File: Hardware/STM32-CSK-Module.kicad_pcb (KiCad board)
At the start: 2 copper layers, 32 parts, among them J1 Conn_Cortex-JTAG-10, U1 STM32F417VGT, X1 8MHz, X2 32.768kHz

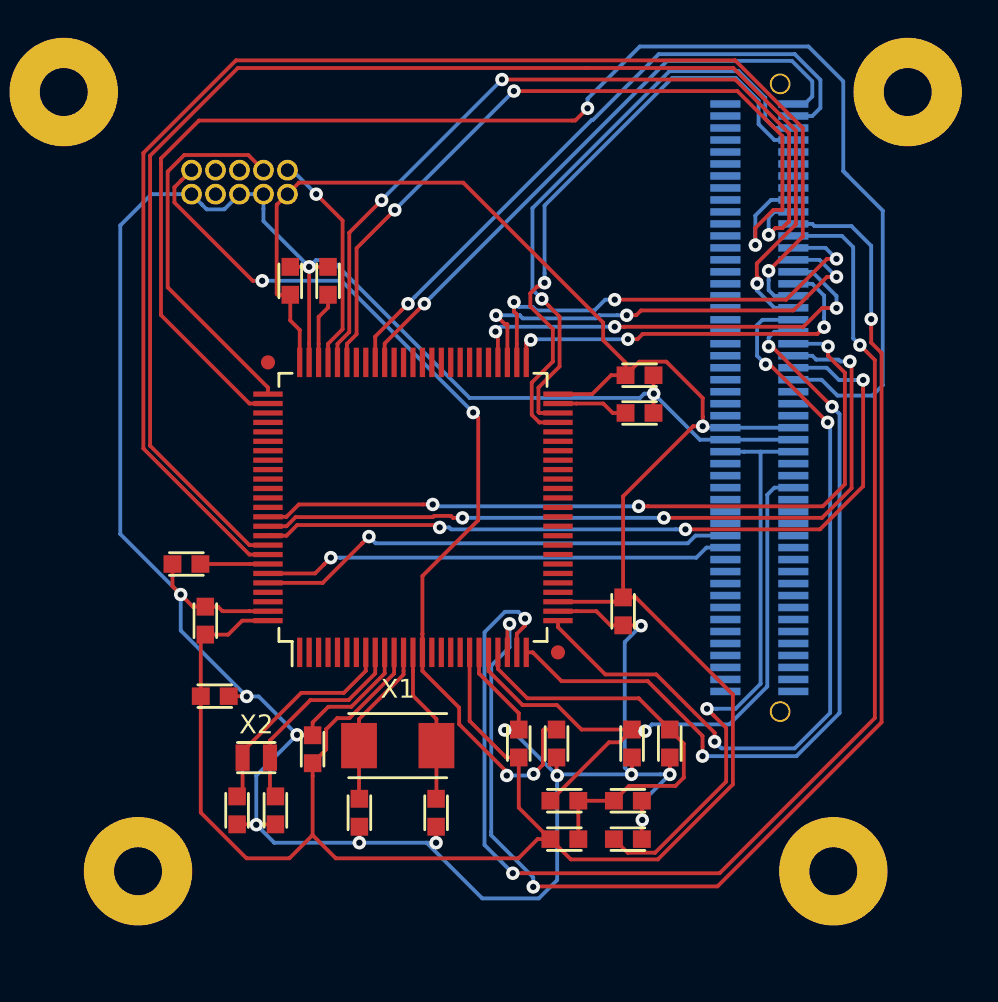
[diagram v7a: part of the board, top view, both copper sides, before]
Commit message: Progress on routing flexible GPIOs
About 50%
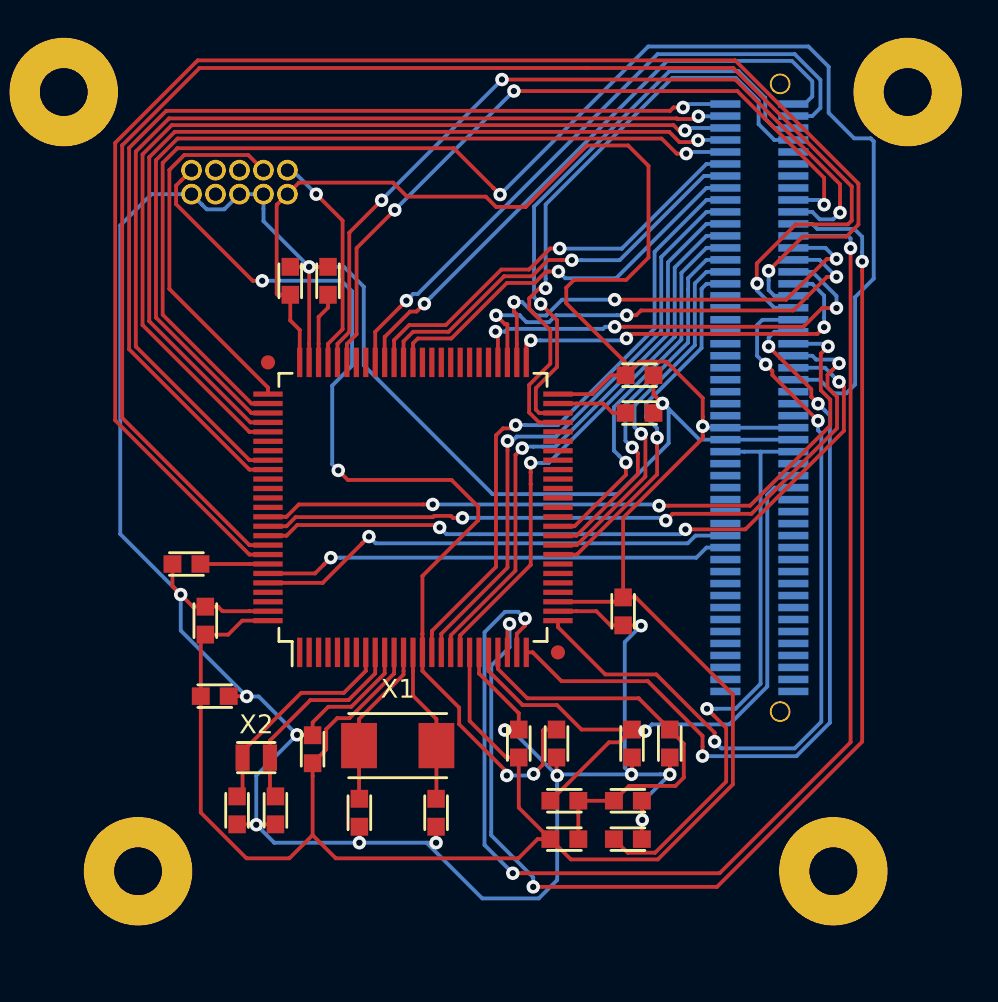
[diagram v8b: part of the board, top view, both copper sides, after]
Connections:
- H1 pad 1: Net-(H1-Pad1) -> /IO47
- H1 pad 10: Net-(H1-Pad10) -> /IO19
- H1 pad 11: Net-(H1-Pad11) -> /IO42
- H1 pad 12: Net-(H1-Pad12) -> /IO18
- H1 pad 13: Net-(H1-Pad13) -> /IO41
- H1 pad 14: Net-(H1-Pad14) -> /IO17
- H1 pad 15: Net-(H1-Pad15) -> /IO40
- H1 pad 16: Net-(H1-Pad16) -> /IO16
- H1 pad 17: Net-(H1-Pad17) -> /AN2
- H1 pad 19: Net-(H1-Pad19) -> /AN3
- H1 pad 21: Net-(H1-Pad21) -> /AN4
- H1 pad 23: Net-(H1-Pad23) -> /AN5
- H1 pad 25: Net-(H1-Pad25) -> /AN1
- H1 pad 27: Net-(H1-Pad27) -> /AN0
- H1 pad 29: Net-(H1-Pad29) -> /AN7
- H1 pad 3: Net-(H1-Pad3) -> /IO46
- H1 pad 31: Net-(H1-Pad31) -> /AN6
- H1 pad 5: Net-(H1-Pad5) -> /IO45
- H1 pad 7: Net-(H1-Pad7) -> /IO44
- H1 pad 9: Net-(H1-Pad9) -> /IO43
- U1 pad 1: Net-(U1-Pad1) -> /IO19
- U1 pad 2: Net-(U1-Pad2) -> /IO18
- U1 pad 3: Net-(U1-Pad3) -> /IO17
- U1 pad 4: Net-(U1-Pad4) -> /IO16
- U1 pad 63: Net-(U1-Pad63) -> /IO40
- U1 pad 64: Net-(U1-Pad64) -> /IO41
- U1 pad 65: Net-(U1-Pad65) -> /IO42
- U1 pad 78: Net-(U1-Pad78) -> /IO43
- U1 pad 79: Net-(U1-Pad79) -> /IO44
- U1 pad 80: Net-(U1-Pad80) -> /IO45
- U1 pad 83: Net-(U1-Pad83) -> /IO46
- U1 pad 84: Net-(U1-Pad84) -> /IO47
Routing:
- net /IO47: track 0.00 -> 53.2 mm, vias 0 -> 1
- net /IO46: track 0.00 -> 51.9 mm, vias 0 -> 1
- net /IO45: track 0.00 -> 49.7 mm, vias 0 -> 1
- net /IO44: track 0.00 -> 48.5 mm, vias 0 -> 1
- net /IO43: track 0.00 -> 47.4 mm, vias 0 -> 1
- net /AN2: track 0.00 -> 32.5 mm, vias 0 -> 1
- net /AN3: track 0.00 -> 31.5 mm, vias 0 -> 1
- net /AN4: track 0.00 -> 30.3 mm, vias 0 -> 1
- net /AN5: track 0.00 -> 29.1 mm, vias 0 -> 1
- net /IO42: track 0.00 -> 22.6 mm, vias 0 -> 1
- net /IO41: track 0.00 -> 21.8 mm, vias 0 -> 1
- net /IO40: track 0.00 -> 21.3 mm, vias 0 -> 1
- net /AN1: track 0.00 -> 20.0 mm, vias 0 -> 1
- net /AN0: track 0.00 -> 20.0 mm, vias 0 -> 1
- net /AN7: track 0.00 -> 19.8 mm, vias 0 -> 1
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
